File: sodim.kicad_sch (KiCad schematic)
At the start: 7 parts, among them J1 Edge_Conn_Bus_DDR5_SODIMM_1xD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, U7 AT24CS01_SOT23

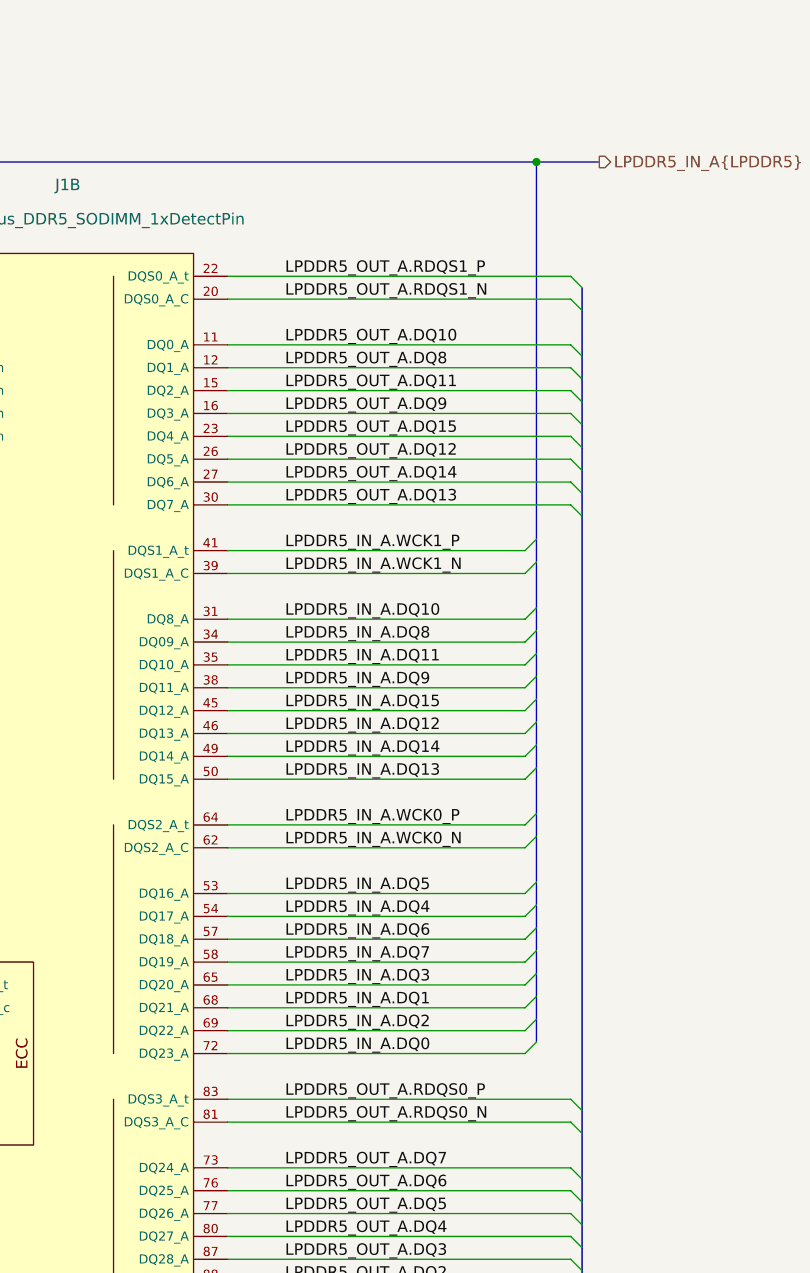
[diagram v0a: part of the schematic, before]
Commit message: [#52835] schematics: replace array resistors with 0402
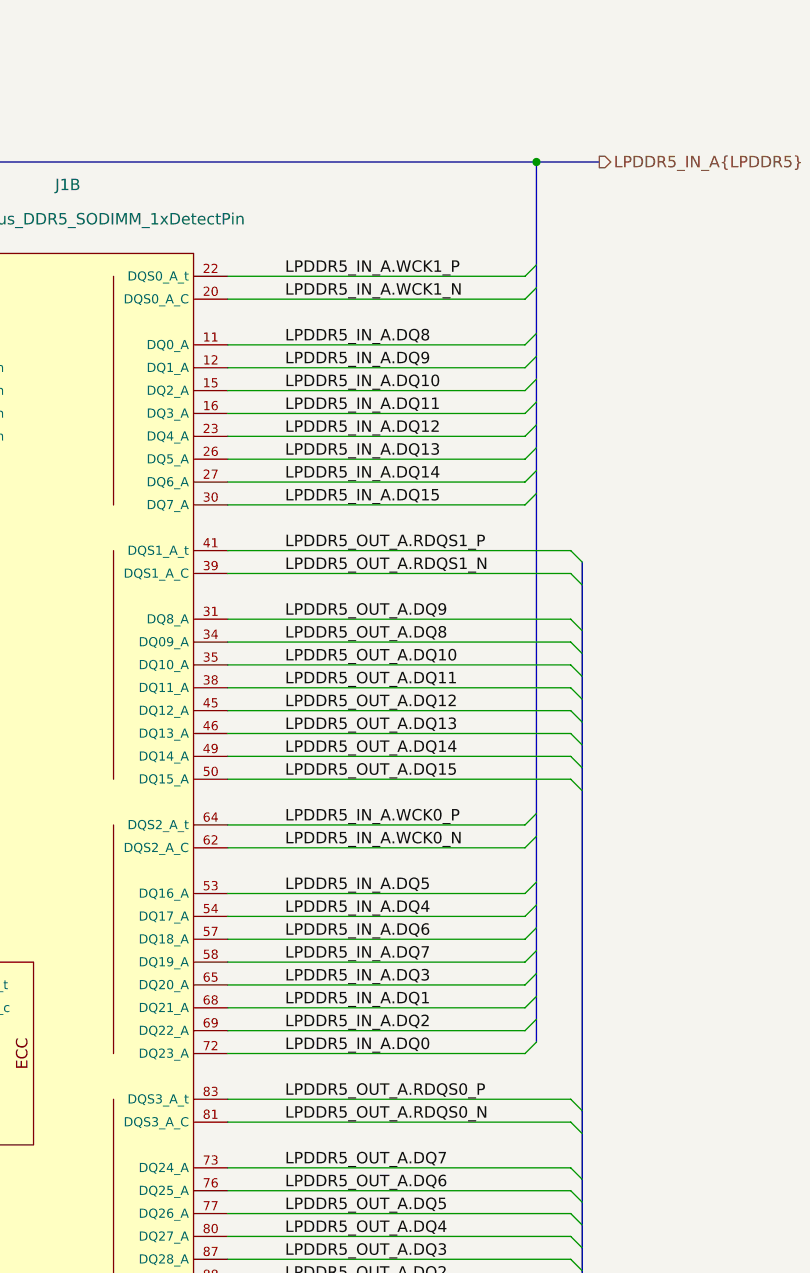
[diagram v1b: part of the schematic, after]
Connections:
- net LPDDR5_IN_A.DQ10: now also J1.15 (DQ2_A); no longer J1.31 (DQ8_A)
- net LPDDR5_IN_A.DQ11: now also J1.16 (DQ3_A); no longer J1.35 (DQ10_A)
- net LPDDR5_IN_A.DQ12: now also J1.23 (DQ4_A); no longer J1.46 (DQ13_A)
- net LPDDR5_IN_A.DQ13: now also J1.26 (DQ5_A); no longer J1.50 (DQ15_A)
- net LPDDR5_IN_A.DQ14: now also J1.27 (DQ6_A); no longer J1.49 (DQ14_A)
- net LPDDR5_IN_A.DQ15: now also J1.30 (DQ7_A); no longer J1.45 (DQ12_A)
- net LPDDR5_IN_A.DQ8: now also J1.11 (DQ0_A); no longer J1.34 (DQ09_A)
- net LPDDR5_IN_A.DQ9: now also J1.12 (DQ1_A); no longer J1.38 (DQ11_A)
- net LPDDR5_IN_A.WCK1_N: now also J1.20 (DQS0_A_C); no longer J1.39 (DQS1_A_C)
- net LPDDR5_IN_A.WCK1_P: now also J1.22 (DQS0_A_t); no longer J1.41 (DQS1_A_t)
- net LPDDR5_OUT_A.DQ10: now also J1.35 (DQ10_A); no longer J1.11 (DQ0_A)
- net LPDDR5_OUT_A.DQ11: now also J1.38 (DQ11_A); no longer J1.15 (DQ2_A)
- net LPDDR5_OUT_A.DQ12: now also J1.45 (DQ12_A); no longer J1.26 (DQ5_A)
- net LPDDR5_OUT_A.DQ13: now also J1.46 (DQ13_A); no longer J1.30 (DQ7_A)
- net LPDDR5_OUT_A.DQ14: now also J1.49 (DQ14_A); no longer J1.27 (DQ6_A)
- net LPDDR5_OUT_A.DQ15: now also J1.50 (DQ15_A); no longer J1.23 (DQ4_A)
- net LPDDR5_OUT_A.DQ8: now also J1.34 (DQ09_A); no longer J1.12 (DQ1_A)
- net LPDDR5_OUT_A.DQ9: now also J1.31 (DQ8_A); no longer J1.16 (DQ3_A)
- net LPDDR5_OUT_A.RDQS1_N: now also J1.39 (DQS1_A_C); no longer J1.20 (DQS0_A_C)
- net LPDDR5_OUT_A.RDQS1_P: now also J1.41 (DQS1_A_t); no longer J1.22 (DQS0_A_t)

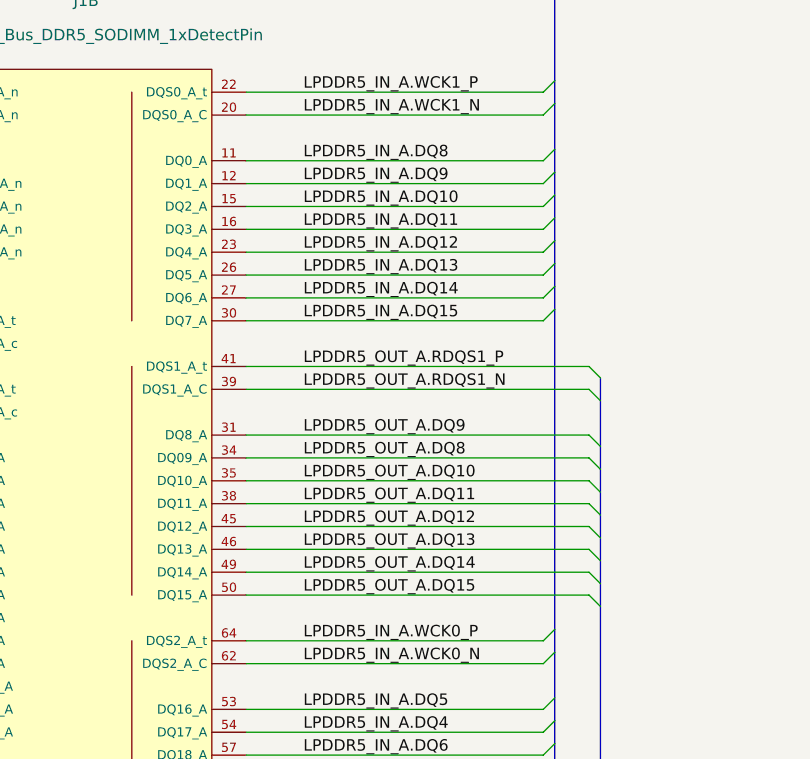
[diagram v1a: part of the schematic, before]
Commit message: [#52974] pcb: poc route using resistor arrays back
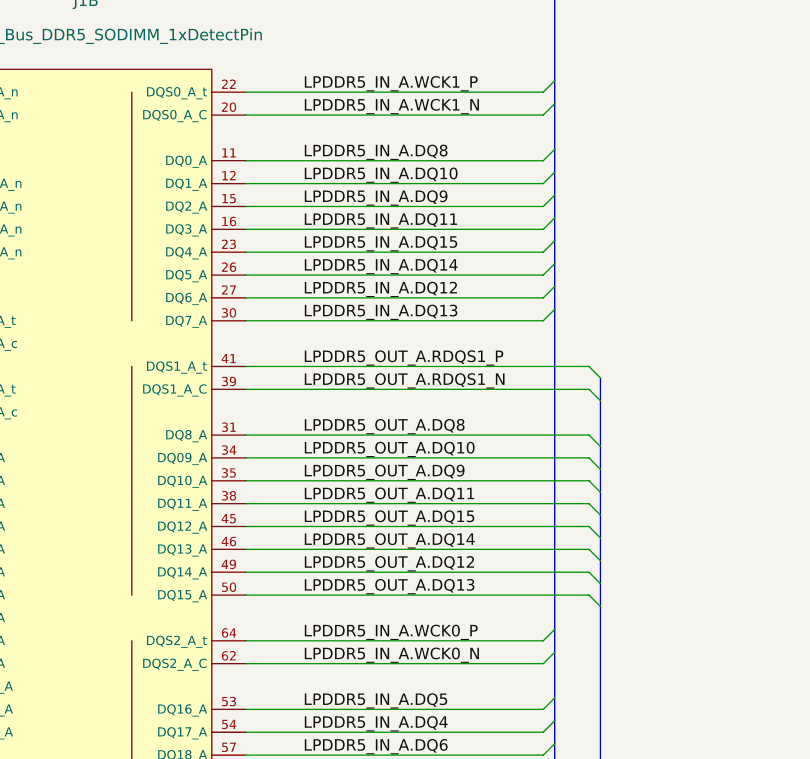
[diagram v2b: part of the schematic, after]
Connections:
- net LPDDR5_IN_A.DQ10: now also J1.12 (DQ1_A); no longer J1.15 (DQ2_A)
- net LPDDR5_IN_A.DQ12: now also J1.27 (DQ6_A); no longer J1.23 (DQ4_A)
- net LPDDR5_IN_A.DQ13: now also J1.30 (DQ7_A); no longer J1.26 (DQ5_A)
- net LPDDR5_IN_A.DQ14: now also J1.26 (DQ5_A); no longer J1.27 (DQ6_A)
- net LPDDR5_IN_A.DQ15: now also J1.23 (DQ4_A); no longer J1.30 (DQ7_A)
- net LPDDR5_IN_A.DQ9: now also J1.15 (DQ2_A); no longer J1.12 (DQ1_A)
- net LPDDR5_OUT_A.DQ10: now also J1.34 (DQ09_A); no longer J1.35 (DQ10_A)
- net LPDDR5_OUT_A.DQ12: now also J1.49 (DQ14_A); no longer J1.45 (DQ12_A)
- net LPDDR5_OUT_A.DQ13: now also J1.50 (DQ15_A); no longer J1.46 (DQ13_A)
- net LPDDR5_OUT_A.DQ14: now also J1.46 (DQ13_A); no longer J1.49 (DQ14_A)
- net LPDDR5_OUT_A.DQ15: now also J1.45 (DQ12_A); no longer J1.50 (DQ15_A)
- net LPDDR5_OUT_A.DQ8: now also J1.31 (DQ8_A); no longer J1.34 (DQ09_A)
- net LPDDR5_OUT_A.DQ9: now also J1.35 (DQ10_A); no longer J1.31 (DQ8_A)
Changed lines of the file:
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@@
     (effects (font (size 1.27 1.27)) (justify left bottom))
   )
-  (label "LPDDR5_OUT_A.DQ14" (at 127 157.48 0)
+  (label "LPDDR5_OUT_A.DQ14" (at 127 154.94 0)
     (effects (font (size 1.27 1.27)) (justify left bottom))
   )
@@
     (effects (font (size 1.27 1.27)) (justify left bottom))
   )
-  (label "LPDDR5_OUT_A.DQ10" (at 127 147.32 0)
+  (label "LPDDR5_OUT_A.DQ10" (at 127 144.78 0)
     (effects (font (size 1.27 1.27)) (justify left bottom))
   )
@@
     (effects (font (size 1.27 1.27)) (justify left bottom))
   )
-  (label "LPDDR5_OUT_A.DQ13" (at 127 154.94 0)
+  (label "LPDDR5_OUT_A.DQ13" (at 127 160.02 0)
     (effects (font (size 1.27 1.27)) (justify left bottom))
   )
@@
     (effects (font (size 1.27 1.27)) (justify left bottom))
   )
-  (label "LPDDR5_OUT_A.DQ8" (at 127 144.78 0)
+  (label "LPDDR5_OUT_A.DQ8" (at 127 142.24 0)
     (effects (font (size 1.27 1.27)) (justify left bottom))
   )
@@
     (effects (font (size 1.27 1.27)) (justify left bottom))
   )
-  (label "LPDDR5_OUT_A.DQ15" (at 127 160.02 0)
+  (label "LPDDR5_OUT_A.DQ15" (at 127 152.4 0)
     (effects (font (size 1.27 1.27)) (justify left bottom))
   )
@@
     (effects (font (size 1.27 1.27)) (justify left bottom))
   )
-  (label "LPDDR5_OUT_A.DQ9" (at 127 142.24 0)
+  (label "LPDDR5_OUT_A.DQ9" (at 127 147.32 0)
     (effects (font (size 1.27 1.27)) (justify left bottom))
   )
@@
     (effects (font (size 1.27 1.27)) (justify left bottom))
   )
-  (label "LPDDR5_IN_A.DQ13" (at 127 124.46 0)
-    (effects (font (size 1.27 1.27)) (justify left bottom))
-  )
-  (label "LPDDR5_IN_A.DQ12" (at 127 121.92 0)
+  (label "LPDDR5_IN_A.DQ13" (at 127 129.54 0)
+    (effects (font (size 1.27 1.27)) (justify left bottom))
+  )
+  (label "LPDDR5_IN_A.DQ12" (at 127 127 0)
     (effects (font (size 1.27 1.27)) (justify left bottom))
   )
@@
     (effects (font (size 1.27 1.27)) (justify left bottom))
   )
-  (label "LPDDR5_IN_A.DQ15" (at 127 129.54 0)
+  (label "LPDDR5_IN_A.DQ15" (at 127 121.92 0)
     (effects (font (size 1.27 1.27)) (justify left bottom))
   )
@@
     (effects (font (size 1.27 1.27)) (justify left bottom))
   )
-  (label "LPDDR5_IN_A.DQ9" (at 127 114.3 0)
+  (label "LPDDR5_IN_A.DQ9" (at 127 116.84 0)
     (effects (font (size 1.27 1.27)) (justify left bottom))
   )
@@
     (effects (font (size 1.27 1.27)) (justify left bottom))
   )
-  (label "LPDDR5_IN_A.DQ14" (at 127 127 0)
+  (label "LPDDR5_IN_A.DQ14" (at 127 124.46 0)
     (effects (font (size 1.27 1.27)) (justify left bottom))
   )
@@
     (effects (font (size 1.27 1.27)) (justify left bottom))
   )
-  (label "LPDDR5_OUT_A.DQ12" (at 127 152.4 0)
+  (label "LPDDR5_OUT_A.DQ12" (at 127 157.48 0)
     (effects (font (size 1.27 1.27)) (justify left bottom))
   )
@@
     (effects (font (size 1.27 1.27)) (justify left bottom))
   )
-  (label "LPDDR5_IN_A.DQ10" (at 127 116.84 0)
-    (effects (font (size 1.27 1.27)) (justify left bottom))
-  )
+  (label "LPDDR5_IN_A.DQ10" (at 127 114.3 0)
+    (effects (font (size 1.27 1.27)) (justify left bottom))
+  )

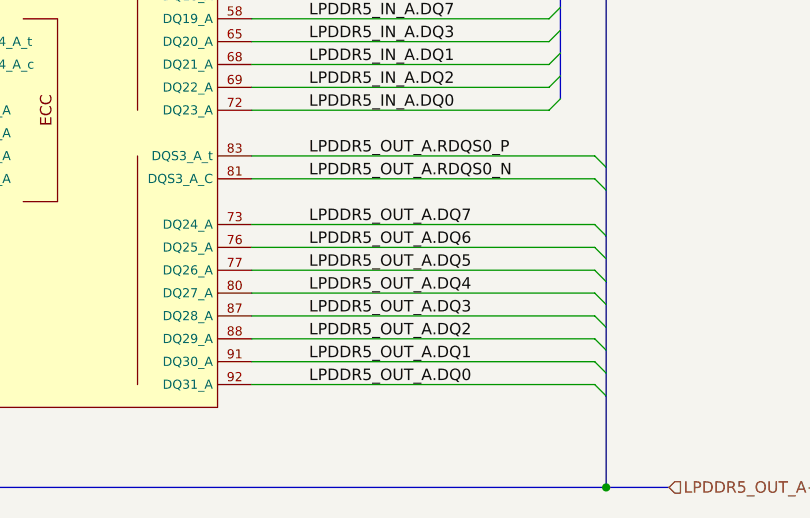
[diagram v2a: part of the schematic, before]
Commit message: [#52974] schematics: final connection of the A side of the die
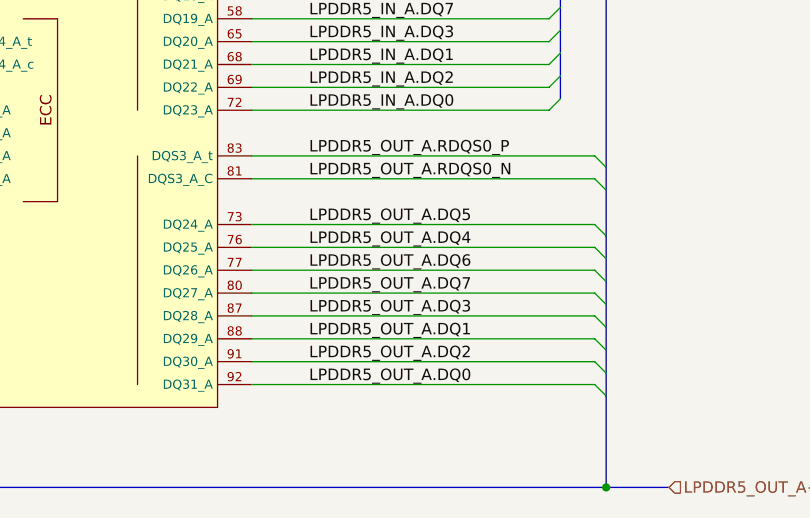
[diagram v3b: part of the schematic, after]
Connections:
- net LPDDR5_OUT_A.DQ1: now also J1.88 (DQ29_A); no longer J1.91 (DQ30_A)
- net LPDDR5_OUT_A.DQ2: now also J1.91 (DQ30_A); no longer J1.88 (DQ29_A)
- net LPDDR5_OUT_A.DQ4: now also J1.76 (DQ25_A); no longer J1.80 (DQ27_A)
- net LPDDR5_OUT_A.DQ5: now also J1.73 (DQ24_A); no longer J1.77 (DQ26_A)
- net LPDDR5_OUT_A.DQ6: now also J1.77 (DQ26_A); no longer J1.76 (DQ25_A)
- net LPDDR5_OUT_A.DQ7: now also J1.80 (DQ27_A); no longer J1.73 (DQ24_A)
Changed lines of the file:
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@@
     (effects (font (size 1.27 1.27)) (justify right bottom))
   )
-  (label "LPDDR5_OUT_A.DQ6" (at 127 205.74 0)
+  (label "LPDDR5_OUT_A.DQ6" (at 127 208.28 0)
     (effects (font (size 1.27 1.27)) (justify left bottom))
   )
@@
     (effects (font (size 1.27 1.27)) (justify left bottom))
   )
-  (label "LPDDR5_OUT_A.DQ1" (at 127 218.44 0)
+  (label "LPDDR5_OUT_A.DQ1" (at 127 215.9 0)
     (effects (font (size 1.27 1.27)) (justify left bottom))
   )
@@
     (effects (font (size 1.27 1.27)) (justify left bottom))
   )
-  (label "LPDDR5_OUT_A.DQ2" (at 127 215.9 0)
+  (label "LPDDR5_OUT_A.DQ2" (at 127 218.44 0)
     (effects (font (size 1.27 1.27)) (justify left bottom))
   )
@@
     (effects (font (size 1.27 1.27)) (justify right bottom))
   )
-  (label "LPDDR5_OUT_A.DQ5" (at 127 208.28 0)
+  (label "LPDDR5_OUT_A.DQ5" (at 127 203.2 0)
     (effects (font (size 1.27 1.27)) (justify left bottom))
   )
@@
     (effects (font (size 1.27 1.27)) (justify left bottom))
   )
-  (label "LPDDR5_OUT_A.DQ4" (at 127 210.82 0)
+  (label "LPDDR5_OUT_A.DQ4" (at 127 205.74 0)
     (effects (font (size 1.27 1.27)) (justify left bottom))
   )
@@
     (effects (font (size 1.27 1.27)) (justify left bottom))
   )
-  (label "LPDDR5_OUT_A.DQ7" (at 127 203.2 0)
-    (effects (font (size 1.27 1.27)) (justify left bottom))
-  )
+  (label "LPDDR5_OUT_A.DQ7" (at 127 210.82 0)
+    (effects (font (size 1.27 1.27)) (justify left bottom))
+  )
